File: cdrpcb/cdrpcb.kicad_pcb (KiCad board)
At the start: 2 copper layers, 119.8 x 90.3 mm, 42 parts, among them J1 Conn_02x04_Odd_Even, J2 Conn_01x03, J3 Conn_01x03, J4 Conn_01x03, J5 Conn_01x03, J6 Conn_01x03, J7 Conn_01x06, J8 Conn_01x04, J9 Conn_01x03, SW1 Conn_01x02_Pin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

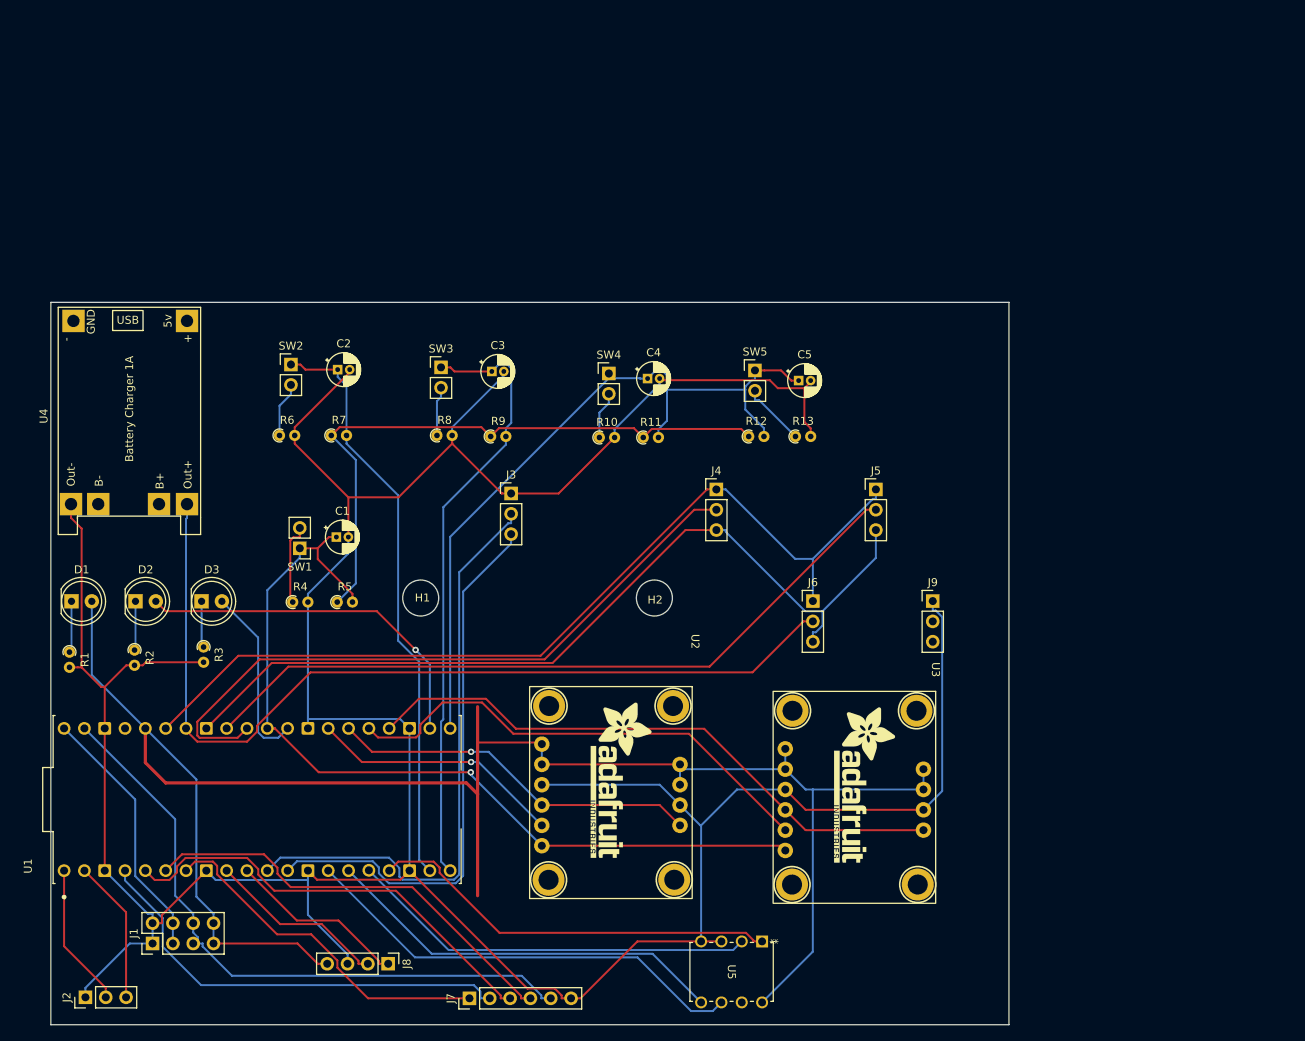
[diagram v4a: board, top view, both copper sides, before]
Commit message: Re-routed with increased pwr/gnd thickness and overall clearance
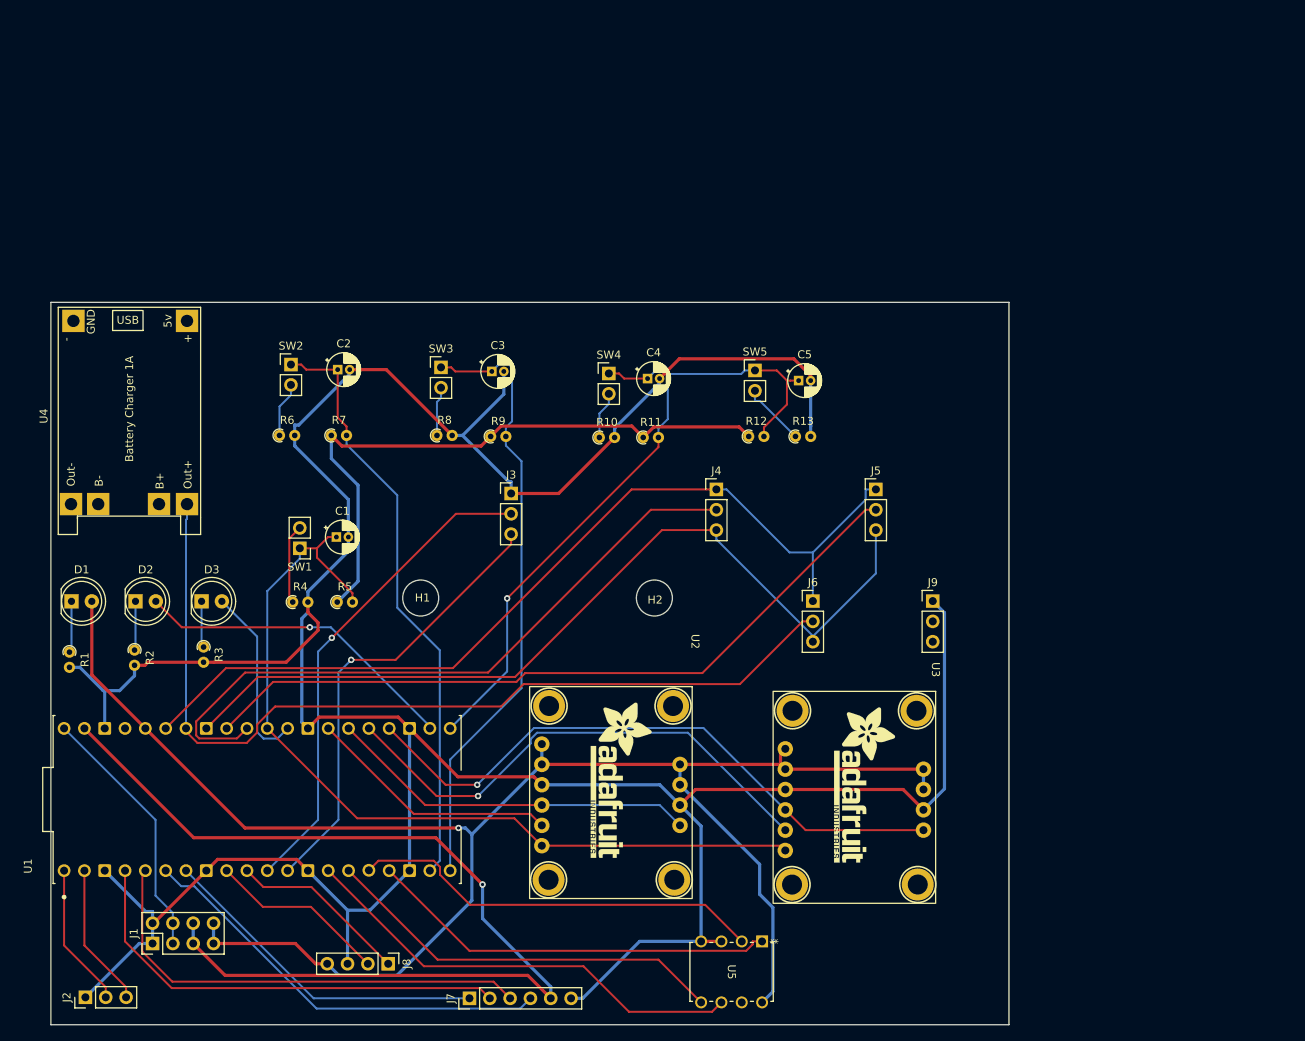
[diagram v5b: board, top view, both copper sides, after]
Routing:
- net +5V: track 80.7 -> 125.7 mm, vias 0 -> 1
- net GND: track 453.8 -> 429.5 mm
- net +3.3V: track 231.7 -> 216.3 mm, vias 0 -> 1
- net /GP8_UART1_TX: track 74.7 -> 61.3 mm, vias 0 -> 1
- net /GP9_UART1_RX: track 69.6 -> 56.9 mm, vias 0 -> 1
- net /SW2: track 94.4 -> 89.1 mm, vias 0 -> 1
- net /LED0: track 45.5 -> 41.0 mm
- net /SPI0_MOSI: track 55.5 -> 58.7 mm
- net /I2C1_SDA: track 75.1 -> 77.9 mm, vias 0 -> 1
- net /I2C1_SCL: track 61.6 -> 64.2 mm, vias 0 -> 1
- net /SPI0_CS: track 44.1 -> 42.0 mm
- net /SPI0_SCK: track 55.5 -> 57.4 mm
- net /SPI0_MISO: track 54.5 -> 53.3 mm
- net /SW0: track 73.5 -> 74.5 mm
- net /SW1: track 76.5 -> 77.4 mm
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
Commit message: add labels, fix charging circuit traces
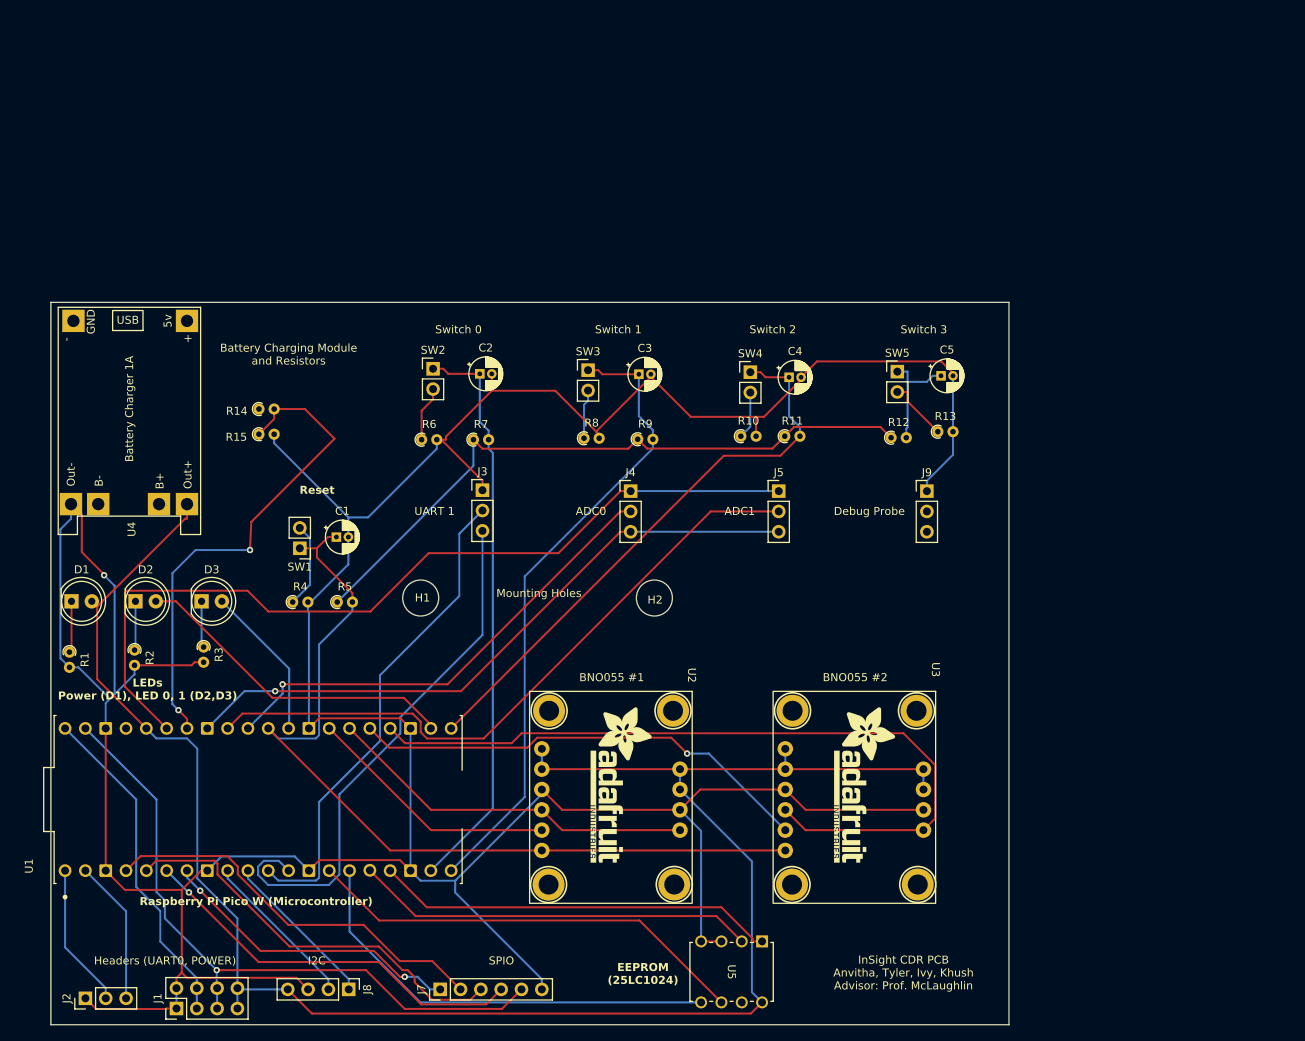
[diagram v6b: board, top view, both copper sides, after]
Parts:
- removed J6: Conn_01x03, Connector_PinHeader_2.54mm:PinHeader_1x03_P2.54mm_Vertical
- added R14: 3.3k, Resistor_THT:R_Axial_DIN0204_L3.6mm_D1.6mm_P1.90mm_Vertical, F.Cu at (86.0, 72.6)
- added R15: 1k, Resistor_THT:R_Axial_DIN0204_L3.6mm_D1.6mm_P1.90mm_Vertical, F.Cu at (86.0, 75.8)
- moved C3 18.4 mm to (133.4, 68.3)
- moved R9 18.4 mm to (133.3, 76.4)
- moved R8 18.4 mm to (126.6, 76.3)
- moved SW3 18.4 mm to (127.1, 67.8)
- moved C5 17.8 mm to (171.2, 68.5)
- moved R13 17.8 mm to (170.8, 75.5)
- moved R12 17.8 mm to (165.0, 76.2)
- moved SW5 17.8 mm to (165.7, 68.0)
- moved C2 17.8 mm to (113.6, 68.2)
- moved R6 17.8 mm to (106.3, 76.5)
- moved R7 17.8 mm to (112.8, 76.5)
- moved SW2 17.8 mm to (107.7, 67.6)
- moved C4 17.7 mm to (152.2, 68.7)
- moved R10 17.7 mm to (146.2, 76.0)
- moved R11 17.7 mm to (151.7, 76.0)
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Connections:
- C5 pad 1: /SW2 -> /SW3
- R12 pad 2: /SW2 -> /SW3
- SW5 pad 1: /SW2 -> /SW3
- U4 pad 1: /GP28_ADC2 -> +3.3V
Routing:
- net GND: track 429.5 -> 486.3 mm, vias 0 -> 1
- net /GP28_ADC2: track 114.3 -> 62.3 mm, vias 0 -> 2
- net +5V: track 125.7 -> 83.0 mm
- net GNDA: track 109.6 -> 81.6 mm, vias 0 -> 1
- net /GP26_ADC0: track 84.8 -> 59.8 mm, vias 0 -> 1
- net /I2C1_SDA: track 77.9 -> 98.1 mm, vias 1 -> 0
- net +3.3V: track 216.3 -> 234.4 mm, vias 1 -> 0
- net /SW2: track 89.1 -> 71.8 mm, vias 1 -> 0
- net /SW3: track 0.00 -> 14.1 mm
- net /GP9_UART1_RX: track 56.9 -> 67.2 mm, vias 1 -> 0
- net VBUS: track 32.5 -> 41.8 mm
- net /GP27_ADC1: track 92.5 -> 83.5 mm
- net /SPI0_MOSI: track 58.7 -> 51.2 mm
- net /SPI0_SCK: track 57.4 -> 50.0 mm
- net VDDA: track 114.5 -> 108.3 mm
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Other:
- board text added: "ADC0"
- board text added: "ADC1"
- board text added: "BNO055 #1"
- board text added: "BNO055 #2"
- board text added: "Battery Charging Module and Resistors"
- board text added: "Debug Probe"
- board text added: "EEPROM (25LC1024)"
- board text added: "Headers (UART0, POWER)"
- board text added: "I2C"
- board text added: "InSight CDR PCB Anvitha, Tyler, Ivy, Khush Advisor: Prof. McLaughlin"
- board text added: "LEDs Power (D1), LED 0, 1 (D2,D3)"
- board text added: "Mounting Holes"
- board text added: "Raspberry Pi Pico W (Microcontroller)"
- board text added: "Reset"
- board text added: "SPIO"
- board text added: "Switch 0"
- board text added: "Switch 1"
- board text added: "Switch 2"
- board text added: "Switch 3"
- board text added: "UART 1"

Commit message: widened traces, fixed charging circuit (for real)
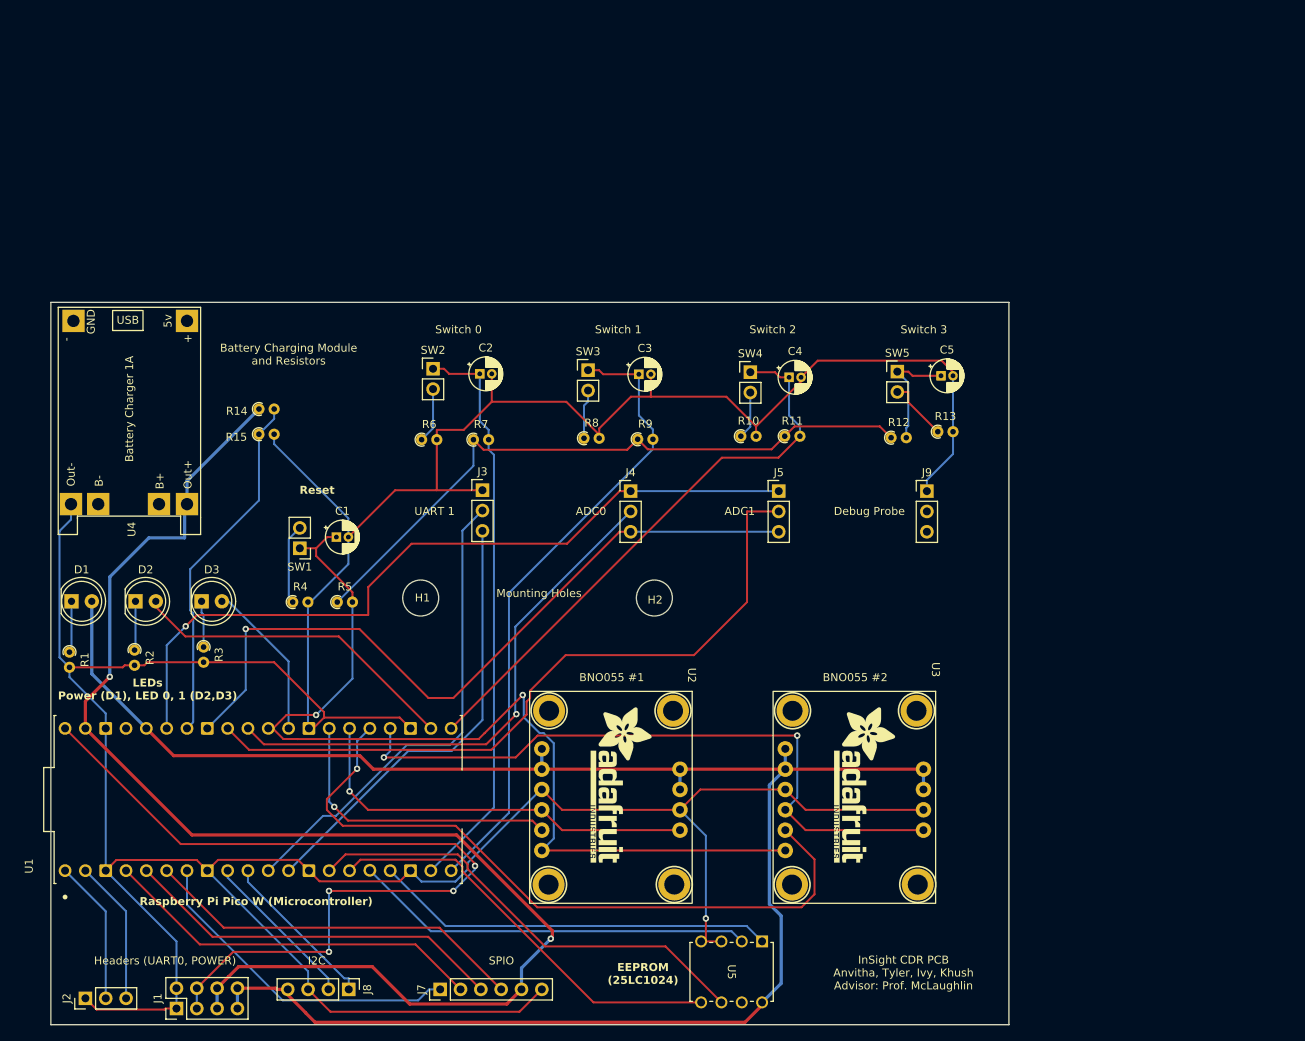
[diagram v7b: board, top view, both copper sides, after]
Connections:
- J1 pad 5: +5V -> VSYS
- J1 pad 6: +5V -> VSYS
- J7 pad 5: +5V -> VSYS
- R14 pad 1: +3.3V -> VSYS
- U1 pad 39: +5V -> VSYS
- U4 pad 1: +3.3V -> VSYS
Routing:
- net VSYS: track 0.00 -> 173.7 mm, vias 0 -> 2
- net +5V: track 83.0 -> 0.00 mm, vias 1 -> 0
- net VBUS: track 41.8 -> 106.9 mm, vias 0 -> 4
- net /I2C1_SCL: track 58.2 -> 88.6 mm
- net /GP28_ADC2: track 62.3 -> 44.7 mm, vias 2 -> 0
- net /I2C1_SDA: track 98.1 -> 85.0 mm, vias 0 -> 2
- net /RST: track 110.1 -> 122.9 mm, vias 0 -> 2
- net GNDA: track 81.6 -> 93.2 mm
- net /GP9_UART1_RX: track 67.2 -> 55.7 mm
- net VDDA: track 108.3 -> 96.9 mm, vias 0 -> 1
- net /GP26_ADC0: track 59.8 -> 67.3 mm
- net /GP27_ADC1: track 83.5 -> 90.5 mm
- net /I2C0_SCL: track 31.8 -> 37.2 mm, vias 0 -> 1
- net /I2C0_SDA: track 46.6 -> 51.2 mm, vias 0 -> 1
- net /SPI0_MOSI: track 51.2 -> 48.0 mm
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
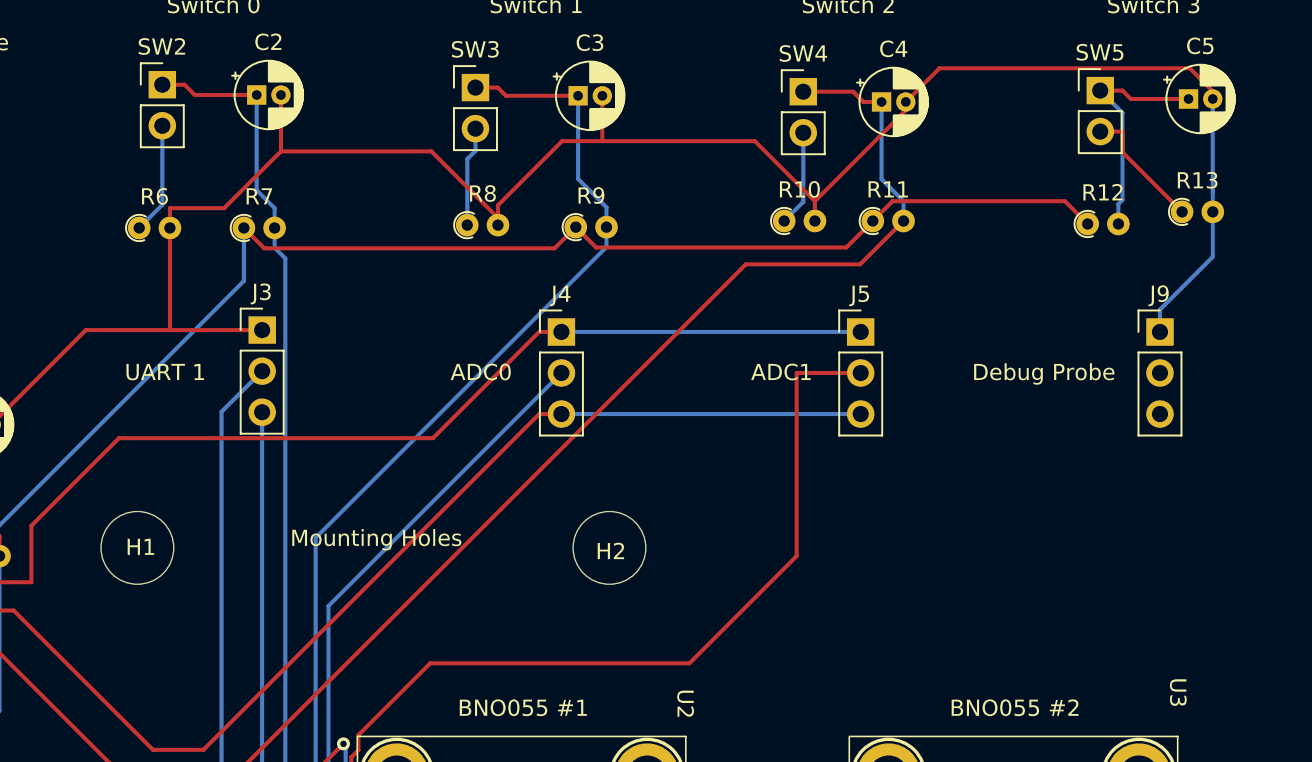
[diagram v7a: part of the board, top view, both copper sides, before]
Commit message: fixing mounting hole distancing and spacing issues and also adding in custom 5.0mm footprint for holes in KiCad
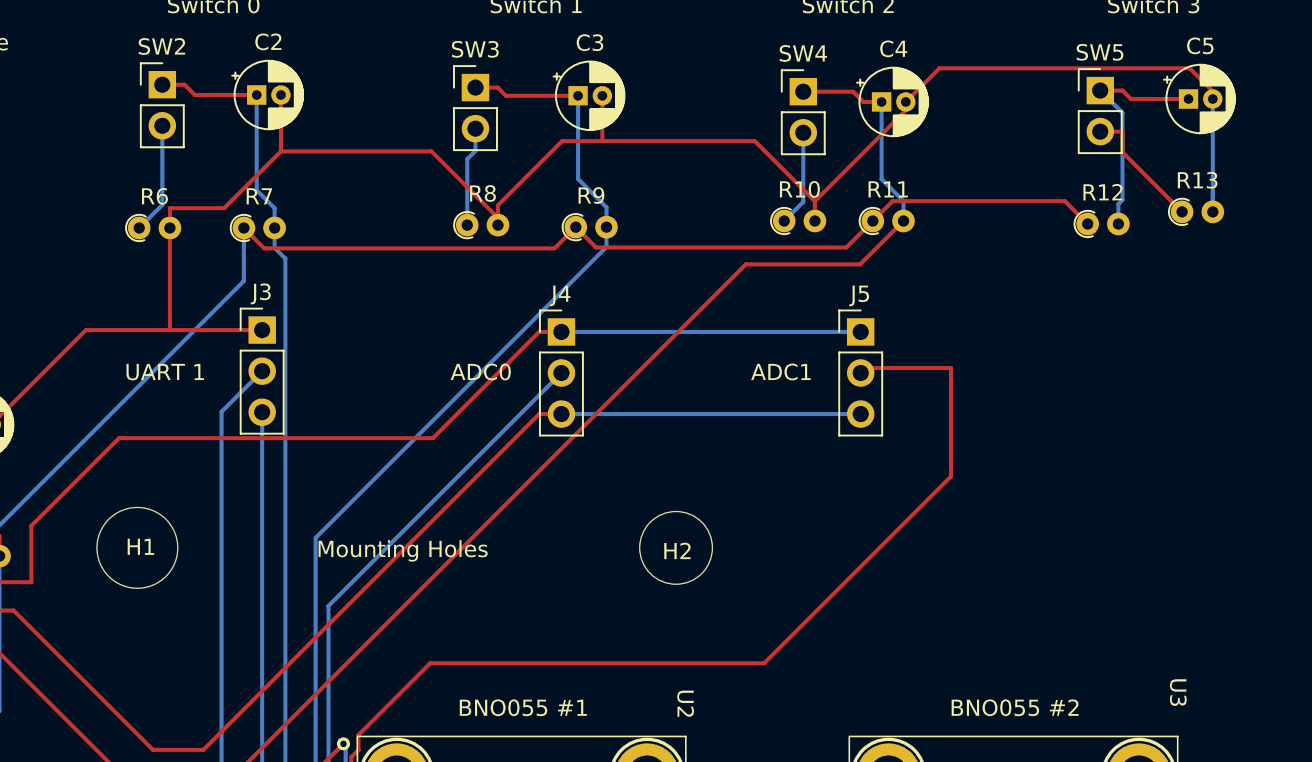
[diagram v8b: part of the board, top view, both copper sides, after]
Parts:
- removed J9: Conn_01x03, Connector_PinHeader_2.54mm:PinHeader_1x03_P2.54mm_Vertical
- H1: footprint MountingHole:MountingHole_4.5mm -> MountingHole:MountingHole_5.0mm
- moved H2 4.12 mm to (139.5, 96.3)
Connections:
- net VSYS renamed +5V
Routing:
- net /GP27_ADC1: track 90.5 -> 99.2 mm
- net GND: track 487.3 -> 479.7 mm
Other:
- board text removed: "Debug Probe"
